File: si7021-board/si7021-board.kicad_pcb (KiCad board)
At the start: 2 copper layers, 9.9 x 45.5 mm, 6 parts, among them U1 SHIELD_I2C, U2 SI7021

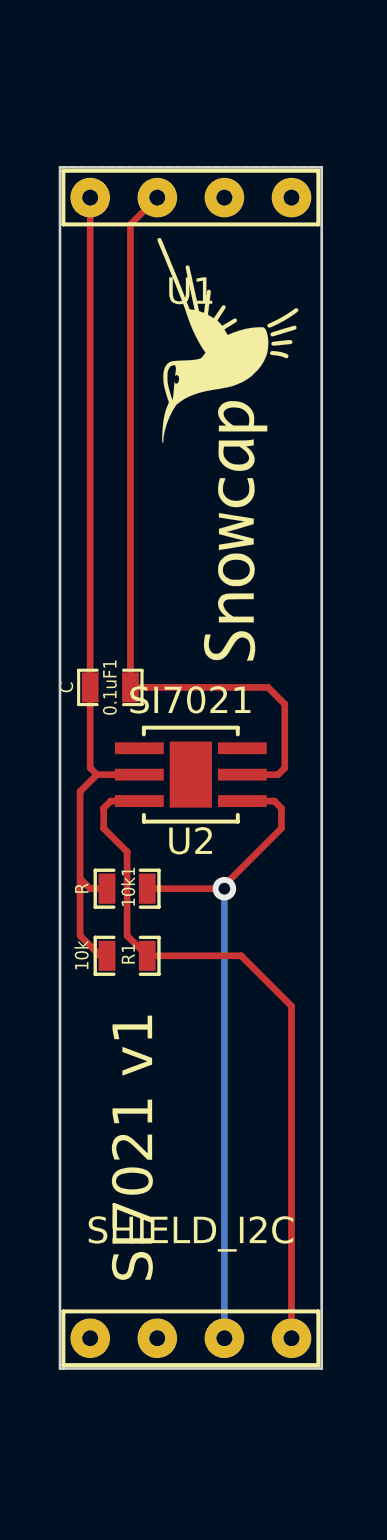
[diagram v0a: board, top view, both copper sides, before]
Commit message: si7021: Add pin names to silk screen
Fix annotation.
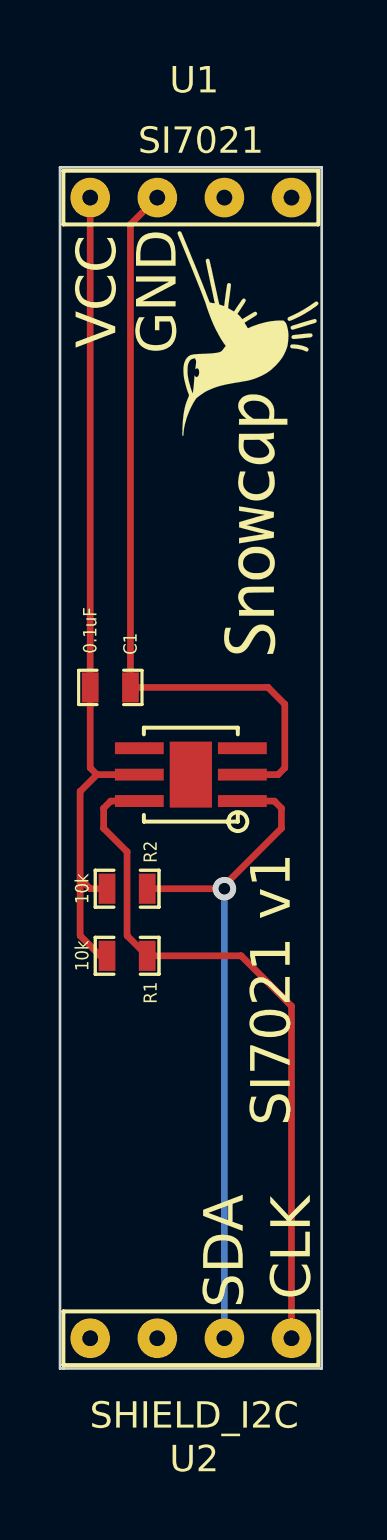
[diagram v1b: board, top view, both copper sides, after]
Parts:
- removed 0.1uF1: C, SM0603_Capa
- removed 10k1: R, SM0603_Resistor
- added C1: 0.1uF, SM0603_Capa, F.Cu at (133.6, 80.8)
- added R2: 10k, SM0603_Resistor, F.Cu at (134.2, 88.4)
- moved ? 0.80 mm to (138.8, 71.5)
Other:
- board text added: "CLK"
- board text added: "GND"
- board text added: "SDA"
- board text added: "VCC"
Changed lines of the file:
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@@
     (links 10)
     (no_connects 0)
-    (area 0 0 0 0)
+    (area 130.803143 56.956 145.635713 110.811)
     (thickness 1.6)
-    (drawings 6)
+    (drawings 10)
     (tracks 35)
     (zones 0)
@@
     (visible_elements FFFFFFBF)
     (pcbplotparams
-      (layerselection 3178497)
+      (layerselection 284196865)
       (usegerberextensions true)
       (excludeedgelayer true)
@@
       (plotreference true)
       (plotvalue true)
-      (plotothertext true)
+      (plotothertext false)
       (plotinvisibletext false)
       (padsonsilk false)
@@
       (outputformat 1)
       (mirror false)
-      (drillshape 1)
+      (drillshape 0)
       (scaleselection 1)
-      (outputdirectory ""))
+      (outputdirectory gerbers/))
   )
   (net 0 "")
@@
     (at 134.239 90.932)
     (attr smd)
-    (fp_text reference R1 (at 0.0635 -0.0635 90) (layer F.SilkS)
+    (fp_text reference R1 (at 0.889 1.397 90) (layer F.SilkS)
       (effects (font (size 0.50038 0.4572) (thickness 0.1143)))
     )
@@
     )
   )
-  (module SM0603_Resistor (layer F.Cu)
-    (at 134.239 88.392)
-    (attr smd)
-    (fp_text reference 10k1 (at 0.0635 -0.0635 90) (layer F.SilkS)
-      (effects (font (size 0.50038 0.4572) (thickness 0.1143)))
-    )
-    (fp_text value R (at -1.69926 0 90) (layer F.SilkS)
-      (effects (font (size 0.508 0.4572) (thickness 0.1143)))
-    )
-    (fp_line (start -0.50038 -0.6985) (end -1.2065 -0.6985) (layer F.SilkS) (width 0.127))
-    (fp_line (start -1.2065 -0.6985) (end -1.2065 0.6985) (layer F.SilkS) (width 0.127))
-    (fp_line (start -1.2065 0.6985) (end -0.50038 0.6985) (layer F.SilkS) (width 0.127))
-    (fp_line (start 1.2065 -0.6985) (end 0.50038 -0.6985) (layer F.SilkS) (width 0.127))
-    (fp_line (start 1.2065 -0.6985) (end 1.2065 0.6985) (layer F.SilkS) (width 0.127))
-    (fp_line (start 1.2065 0.6985) (end 0.50038 0.6985) (layer F.SilkS) (width 0.127))
-    (pad 1 smd rect (at -0.762 0) (size 0.635 1.143)
-      (layers F.Cu F.Paste F.Mask)
-      (net 4 VCC)
-    )
-    (pad 2 smd rect (at 0.762 0) (size 0.635 1.143)
-      (layers F.Cu F.Paste F.Mask)
-      (net 3 N-000008)
-    )
-    (model smd\resistors\R0603.wrl
-      (at (xyz 0 0 0.001))
-      (scale (xyz 0.5 0.5 0.5))
-      (rotate (xyz 0 0 0))
-    )
-  )
-  (module SM0603_Capa (layer F.Cu)
-    (at 133.604 80.772)
-    (attr smd)
-    (fp_text reference 0.1uF1 (at 0 0 90) (layer F.SilkS)
-      (effects (font (size 0.508 0.4572) (thickness 0.1143)))
-    )
-    (fp_text value C (at -1.651 0 90) (layer F.SilkS)
-      (effects (font (size 0.508 0.4572) (thickness 0.1143)))
-    )
-    (fp_line (start 0.50038 0.65024) (end 1.19888 0.65024) (layer F.SilkS) (width 0.11938))
-    (fp_line (start -0.50038 0.65024) (end -1.19888 0.65024) (layer F.SilkS) (width 0.11938))
-    (fp_line (start 0.50038 -0.65024) (end 1.19888 -0.65024) (layer F.SilkS) (width 0.11938))
-    (fp_line (start -1.19888 -0.65024) (end -0.50038 -0.65024) (layer F.SilkS) (width 0.11938))
-    (fp_line (start 1.19888 -0.635) (end 1.19888 0.635) (layer F.SilkS) (width 0.11938))
-    (fp_line (start -1.19888 0.635) (end -1.19888 -0.635) (layer F.SilkS) (width 0.11938))
-    (pad 1 smd rect (at -0.762 0) (size 0.635 1.143)
-      (layers F.Cu F.Paste F.Mask)
-      (net 4 VCC)
-    )
-    (pad 2 smd rect (at 0.762 0) (size 0.635 1.143)
-      (layers F.Cu F.Paste F.Mask)
-      (net 1 GND)
-    )
-    (model smd\capacitors\C0603.wrl
-      (at (xyz 0 0 0.001))
-      (scale (xyz 0.5 0.5 0.5))
-      (rotate (xyz 0 0 0))
-    )
-  )
   (module SHIELD_I2C (layer F.Cu)
     (at 136.652 83.82)
-    (fp_text reference U1 (at 0 -18.034) (layer F.SilkS)
+    (fp_text reference U1 (at 0.127 -26.035) (layer F.SilkS)
       (effects (font (size 1 1) (thickness 0.15)))
     )
-    (fp_text value SHIELD_I2C (at 0 17.526) (layer F.SilkS)
+    (fp_text value SHIELD_I2C (at 0.127 24.511) (layer F.SilkS)
       (effects (font (size 1 1) (thickness 0.15)))
     )
@@
     (at 136.652 84.074 180)
     (clearance 0.1)
-    (fp_text reference U2 (at 0 -2.54 180) (layer F.SilkS)
+    (fp_text reference U2 (at -0.127 -25.908 180) (layer F.SilkS)
       (effects (font (size 1 1) (thickness 0.15)))
     )
-    (fp_text value SI7021 (at 0 2.794 180) (layer F.SilkS)
+    (fp_text value SI7021 (at -0.381 24.003 180) (layer F.SilkS)
       (effects (font (size 1 1) (thickness 0.15)))
     )
+    (fp_circle (center -1.778 -1.778) (end -2.032 -2.032) (layer F.SilkS) (width 0.15))
     (fp_line (start -1.778 1.524) (end -1.778 1.778) (layer F.SilkS) (width 0.15))
     (fp_line (start -1.778 1.778) (end 1.778 1.778) (layer F.SilkS) (width 0.15))
@@
     )
   )
+  (module SM0603_Resistor (layer F.Cu)
+    (at 134.239 88.392)
+    (attr smd)
+    (fp_text reference R2 (at 0.889 -1.397 90) (layer F.SilkS)
+      (effects (font (size 0.50038 0.4572) (thickness 0.1143)))
+    )
+    (fp_text value 10k (at -1.69926 0 90) (layer F.SilkS)
+      (effects (font (size 0.508 0.4572) (thickness 0.1143)))
+    )
+    (fp_line (start -0.50038 -0.6985) (end -1.2065 -0.6985) (layer F.SilkS) (width 0.127))
+    (fp_line (start -1.2065 -0.6985) (end -1.2065 0.6985) (layer F.SilkS) (width 0.127))
+    (fp_line (start -1.2065 0.6985) (end -0.50038 0.6985) (layer F.SilkS) (width 0.127))
+    (fp_line (start 1.2065 -0.6985) (end 0.50038 -0.6985) (layer F.SilkS) (width 0.127))
+    (fp_line (start 1.2065 -0.6985) (end 1.2065 0.6985) (layer F.SilkS) (width 0.127))
+    (fp_line (start 1.2065 0.6985) (end 0.50038 0.6985) (layer F.SilkS) (width 0.127))
+    (pad 1 smd rect (at -0.762 0) (size 0.635 1.143)
+      (layers F.Cu F.Paste F.Mask)
+      (net 4 VCC)
+    )
+    (pad 2 smd rect (at 0.762 0) (size 0.635 1.143)
+      (layers F.Cu F.Paste F.Mask)
+      (net 3 N-000008)
+    )
+    (model smd\resistors\R0603.wrl
+      (at (xyz 0 0 0.001))
+      (scale (xyz 0.5 0.5 0.5))
+      (rotate (xyz 0 0 0))
+    )
+  )
+  (module SM0603_Capa (layer F.Cu)
+    (at 133.604 80.772)
+    (attr smd)
+    (fp_text reference C1 (at 0.762 -1.651 90) (layer F.SilkS)
+      (effects (font (size 0.508 0.4572) (thickness 0.1143)))
+    )
+    (fp_text value 0.1uF (at -0.762 -2.159 90) (layer F.SilkS)
+      (effects (font (size 0.508 0.4572) (thickness 0.1143)))
+    )
+    (fp_line (start 0.50038 0.65024) (end 1.19888 0.65024) (layer F.SilkS) (width 0.11938))
+    (fp_line (start -0.50038 0.65024) (end -1.19888 0.65024) (layer F.SilkS) (width 0.11938))
+    (fp_line (start 0.50038 -0.65024) (end 1.19888 -0.65024) (layer F.SilkS) (width 0.11938))
+    (fp_line (start -1.19888 -0.65024) (end -0.50038 -0.65024) (layer F.SilkS) (width 0.11938))
+    (fp_line (start 1.19888 -0.635) (end 1.19888 0.635) (layer F.SilkS) (width 0.11938))
+    (fp_line (start -1.19888 0.635) (end -1.19888 -0.635) (layer F.SilkS) (width 0.11938))
+    (pad 1 smd rect (at -0.762 0) (size 0.635 1.143)
+      (layers F.Cu F.Paste F.Mask)
+      (net 4 VCC)
+    )
+    (pad 2 smd rect (at 0.762 0) (size 0.635 1.143)
+      (layers F.Cu F.Paste F.Mask)
+      (net 1 GND)
+    )
+    (model smd\capacitors\C0603.wrl
+      (at (xyz 0 0 0.001))
+      (scale (xyz 0.5 0.5 0.5))
+      (rotate (xyz 0 0 0))
+    )
+  )
   (module LOGO_SNOWCAP_FRONT (layer F.Cu)
-    (at 138.049 71.755 90)
+    (at 138.811 71.501 90)
     (fp_text reference "" (at 0 0 90) (layer F.SilkS) hide
       (effects (font (size 1.524 1.524) (thickness 0.3048)))
@@
       (xy -2.41808 -0.3302) (xy -2.41808 -0.3302)) (layer F.SilkS) (width 0.00254))
   )
-  (gr_text "SI7021 v1" (at 134.493 98.171 90) (layer F.SilkS)
+  (gr_text CLK (at 140.462 101.981 90) (layer F.SilkS)
     (effects (font (size 1.5 1.5) (thickness 0.3)))
   )
+  (gr_text SDA (at 137.922 102.108 90) (layer F.SilkS)
+    (effects (font (size 1.5 1.5) (thickness 0.3)))
+  )
+  (gr_text GND (at 135.382 65.786 90) (layer F.SilkS)
+    (effects (font (size 1.5 1.5) (thickness 0.3)))
+  )
+  (gr_text VCC (at 133.096 65.786 90) (layer F.SilkS)
+    (effects (font (size 1.5 1.5) (thickness 0.3)))
+  )
+  (gr_text "SI7021 v1" (at 139.7 92.202 90) (layer F.SilkS)
+    (effects (font (size 1.5 1.5) (thickness 0.3)))
+  )
